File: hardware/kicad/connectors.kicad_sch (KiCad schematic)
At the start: 4 parts, among them J3 Magnetic USB (Adafruit 5358):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, J4 Battery JST-PH (Adafruit 1570), U7 USBLC6-2SC6

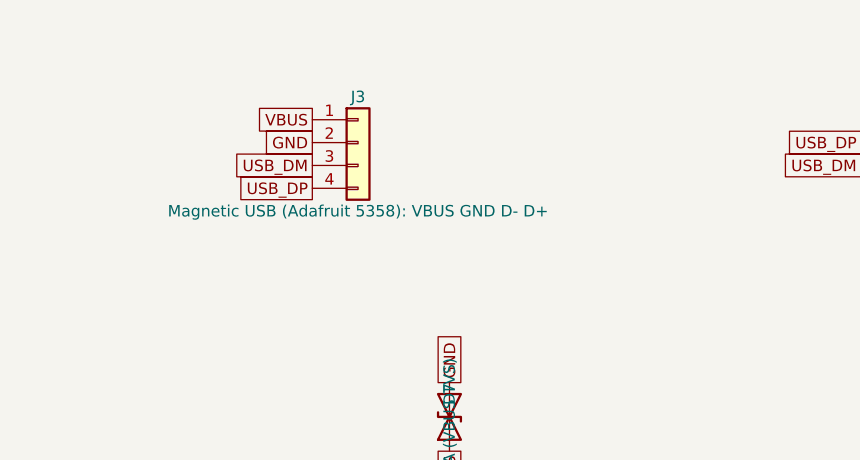
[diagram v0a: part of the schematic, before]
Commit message: Final review, v14 order prep, firmware fixes and production planning
- PCB v14 confirmed GO by final reviews (verification 06, 08, 11)
- CAD fit rev G with measured rib/pin/hook heights; grind zones 6, 6b, 6c
- Firmware: OTA updates, phone setup portal, low-battery gate, polish
- Docs: arrival checklist, vendor comparison, order walkthrough updates
- Production: QA test plan, knockoff shell plan, cost model

Co-Authored-By: Claude Opus 5.5 <noreply@anthropic.com>
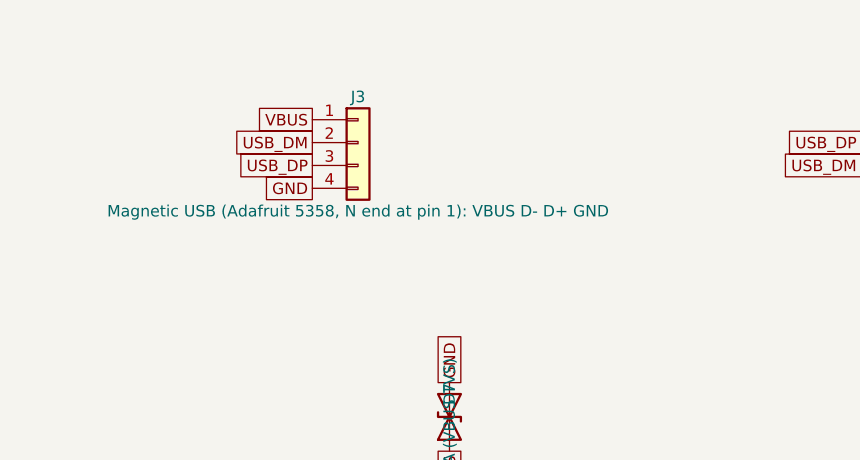
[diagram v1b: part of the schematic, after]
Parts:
- J3: value Magnetic USB (Adafruit 5358): VBUS GND D- D+ -> Magnetic USB (Adafruit 5358, N end at pin 1): VBUS D- D+ GND; footprint ai_calc:PinSocket_1x04_P2.54mm_SMD_H5.0_C42379197 -> ai_calc:PinSocket_1x04_P2.54mm_SMD_RA_C46061768; LCSC C42379197 -> C46061768; MPN HX PM2.54-1x4P TP-YQ (5 mm SMD female header) -> HX PM2.54-1x4P WT (right-angle SMD female header)
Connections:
- net GND: now also J3.4 (Pin_4); no longer J3.2 (Pin_2)
- net USB_DM: now also J3.2 (Pin_2); no longer J3.3 (Pin_3)
- net USB_DP: now also J3.3 (Pin_3); no longer J3.4 (Pin_4)
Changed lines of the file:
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@@
 			)
 		)
-		(property "Value" "Magnetic USB (Adafruit 5358): VBUS GND D- D+"
+		(property "Value" "Magnetic USB (Adafruit 5358, N end at pin 1): VBUS D- D+ GND"
 			(at 49.53 67.31 0)
 			(show_name no)
@@
 			)
 		)
-		(property "Footprint" "ai_calc:PinSocket_1x04_P2.54mm_SMD_H5.0_C42379197"
-			(at 49.53 59.69 0)
-			(hide yes)
-			(show_name no)
-			(do_not_autoplace no)
-			(effects
-				(font
-					(size 1.27 1.27)
-				)
-			)
-		)
-		(property "Datasheet" ""
+		(property "Footprint" "ai_calc:PinSocket_1x04_P2.54mm_SMD_RA_C46061768"
+			(at 49.53 59.69 0)
+			(hide yes)
+			(show_name no)
+			(do_not_autoplace no)
+			(effects
+				(font
+					(size 1.27 1.27)
+				)
+			)
+		)
+		(property "Datasheet" "https://www.lcsc.com/datasheet/C46061768.pdf"
 			(at 49.53 59.69 0)
 			(hide yes)
@@
 			)
 		)
-		(property "LCSC" "C42379197"
-			(at 49.53 59.69 0)
-			(hide yes)
-			(show_name no)
-			(do_not_autoplace no)
-			(effects
-				(font
-					(size 1.27 1.27)
-				)
-			)
-		)
-		(property "MPN" "HX PM2.54-1x4P TP-YQ (5 mm SMD female header)"
+		(property "LCSC" "C46061768"
+			(at 49.53 59.69 0)
+			(hide yes)
+			(show_name no)
+			(do_not_autoplace no)
+			(effects
+				(font
+					(size 1.27 1.27)
+				)
+			)
+		)
+		(property "MPN" "HX PM2.54-1x4P WT (right-angle SMD female header)"
 			(at 49.53 59.69 0)
 			(hide yes)
@@
 		)
 	)
-	(global_label "GND"
+	(global_label "USB_DM"
 		(at 44.45 59.69 180)
 		(effects
@@
 		)
 	)
-	(global_label "USB_DM"
+	(global_label "USB_DP"
 		(at 44.45 62.23 180)
 		(effects
@@
 		)
 	)
-	(global_label "USB_DP"
+	(global_label "GND"
 		(at 44.45 64.77 180)
 		(effects
